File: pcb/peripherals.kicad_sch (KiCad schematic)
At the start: 12 parts, among them J10 SPI, J14 SERIAL, J3 INDICATOR, J8 QWIIC1, J9 QWIIC2, Q1 MMBT2222A

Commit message: Cleaned up fab layer. Minor tweaks. Updated renders.
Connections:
- net GND: now also J14.3; no longer J14.1
- net RX: now also J14.2; no longer J14.3
- net TX: now also J14.1; no longer J14.2
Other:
- moved on the sheet: J9
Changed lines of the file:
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@@
-	(wire
-		(pts
-			(xy 116.84 30.48) (xy 125.73 30.48)
-		)
-		(stroke
-			(width 0)
-			(type default)
-		)
-	)
 	(wire
 		(pts
@@
 	(wire
 		(pts
-			(xy 116.84 27.94) (xy 125.73 27.94)
-		)
-		(stroke
-			(width 0)
-			(type default)
-		)
-	)
-	(wire
-		(pts
 			(xy 238.76 38.1) (xy 238.76 39.37)
 		)
@@
 	(wire
 		(pts
+			(xy 116.84 30.48) (xy 124.46 30.48)
+		)
+		(stroke
+			(width 0)
+			(type default)
+		)
+	)
+	(wire
+		(pts
 			(xy 110.49 96.52) (xy 120.65 96.52)
 		)
@@
 	(wire
 		(pts
+			(xy 116.84 27.94) (xy 121.92 27.94)
+		)
+		(stroke
+			(width 0)
+			(type default)
+		)
+	)
+	(wire
+		(pts
 			(xy 207.01 60.96) (xy 207.01 67.31)
 		)
@@
 	(wire
 		(pts
-			(xy 54.61 54.61) (xy 68.58 54.61)
+			(xy 49.53 54.61) (xy 68.58 54.61)
 		)
 		(stroke
@@
 	(wire
 		(pts
-			(xy 54.61 52.07) (xy 68.58 52.07)
+			(xy 49.53 52.07) (xy 68.58 52.07)
+		)
+		(stroke
+			(width 0)
+			(type default)
+		)
+	)
+	(wire
+		(pts
+			(xy 116.84 25.4) (xy 121.92 25.4)
 		)
 		(stroke
@@
 	(global_label "RX"
 		(shape output)
-		(at 125.73 30.48 0)
+		(at 121.92 27.94 0)
 		(fields_autoplaced yes)
 		(effects
@@
 		)
 		(property "Intersheetrefs" "${INTERSHEET_REFS}"
-			(at 131.1947 30.48 0)
+			(at 127.3847 27.94 0)
 			(effects
 				(font
@@
 	(global_label "TX"
 		(shape input)
-		(at 125.73 27.94 0)
-		(fields_autoplaced yes)
+		(at 121.92 25.4 0)
 		(effects
 			(font
@@
 		)
 		(property "Intersheetrefs" "${INTERSHEET_REFS}"
-			(at 130.8923 27.94 0)
+			(at 126.492 25.4 0)
 			(effects
 				(font
@@
 	(symbol
 		(lib_id "power:GND")
-		(at 116.84 25.4 90)
+		(at 124.46 30.48 90)
 		(unit 1)
 		(exclude_from_sim no)
@@
 		(on_board yes)
 		(dnp no)
-		(fields_autoplaced yes)
 		(property "Reference" "#PWR028"
-			(at 123.19 25.4 0)
+			(at 130.81 30.48 0)
 			(effects
 				(font
@@
 		)
 		(property "Value" "GND"
-			(at 120.65 25.3999 90)
+			(at 127.762 30.48 90)
 			(effects
 				(font
@@
 		)
 		(property "Footprint" ""
-			(at 116.84 25.4 0)
+			(at 124.46 30.48 0)
 			(effects
 				(font
@@
 		)
 		(property "Datasheet" ""
-			(at 116.84 25.4 0)
+			(at 124.46 30.48 0)
 			(effects
 				(font
@@
 		)
 		(property "Description" "Power symbol creates a global label with name \"GND\" , ground"
-			(at 116.84 25.4 0)
+			(at 124.46 30.48 0)
 			(effects
 				(font
@@
 	(symbol
 		(lib_id "power:+3.3V")
-		(at 54.61 57.15 270)
+		(at 49.53 57.15 270)
 		(unit 1)
 		(exclude_from_sim no)
@@
 		(fields_autoplaced yes)
 		(property "Reference" "#PWR077"
-			(at 50.8 57.15 0)
+			(at 45.72 57.15 0)
 			(effects
 				(font
@@
 		)
 		(property "Value" "+3.3V"
-			(at 58.42 57.1499 90)
+			(at 53.34 57.1499 90)
 			(effects
 				(font
@@
 		)
 		(property "Footprint" ""
-			(at 54.61 57.15 0)
+			(at 49.53 57.15 0)
 			(effects
 				(font
@@
 		)
 		(property "Datasheet" ""
-			(at 54.61 57.15 0)
+			(at 49.53 57.15 0)
 			(effects
 				(font
@@
 		)
 		(property "Description" "Power symbol creates a global label with name \"+3.3V\""
-			(at 54.61 57.15 0)
+			(at 49.53 57.15 0)
 			(effects
 				(font
@@
 	(symbol
 		(lib_id "CRGM Connector:QWIIC")
-		(at 41.91 49.53 0)
+		(at 36.83 49.53 0)
 		(unit 1)
 		(exclude_from_sim no)
@@
 		(dnp no)
 		(property "Reference" "J9"
-			(at 46.482 45.72 0)
+			(at 41.402 45.72 0)
 			(effects
 				(font
@@
 		)
 		(property "Value" "QWIIC2"
-			(at 46.355 48.26 0)
+			(at 41.275 48.26 0)
 			(effects
 				(font
@@
 		)
 		(property "Footprint" "CRGM Connector:JST_SH_BM04B-SRSS-TB_1x04-1MP_P1.00mm_Vertical"
-			(at 41.91 49.53 0)
+			(at 36.83 49.53 0)
 			(effects
 				(font
@@
 		)
 		(property "Datasheet" "https://jlcpcb.com/partdetail/Hdgc-1_0K_BH4PB/C2919601"
-			(at 41.91 49.53 0)
+			(at 36.83 49.53 0)
 			(effects
 				(font
@@
 		)
 		(property "Description" "JST SH 1.0mm 4 Position Vertical"
-			(at 41.91 49.53 0)
+			(at 36.83 49.53 0)
 			(effects
 				(font
@@
 		)
 		(property "MPN" "BM04B-SRSS-TB"
-			(at 41.91 49.53 0)
+			(at 36.83 49.53 0)
 			(effects
 				(font
@@
 		)
 		(property "MN" "JST"
-			(at 41.91 49.53 0)
+			(at 36.83 49.53 0)
 			(effects
 				(font
@@
 		)
 		(property "LCSC" "C2919601"
-			(at 41.91 49.53 0)
+			(at 36.83 49.53 0)
 			(effects
 				(font
@@
 		)
 		(property "Mouser" "306-BM04BSRSSTBTLFSN"
-			(at 41.91 49.53 0)
+			(at 36.83 49.53 0)
 			(effects
 				(font
@@
 		)
 		(property "Digikey" "455-BM04B-SRSS-TBTR-ND"
-			(at 41.91 49.53 0)
+			(at 36.83 49.53 0)
 			(effects
 				(font
@@
 	(symbol
 		(lib_id "power:GND")
-		(at 54.61 59.69 90)
+		(at 49.53 59.69 90)
 		(unit 1)
 		(exclude_from_sim no)
@@
 		(fields_autoplaced yes)
 		(property "Reference" "#PWR078"
-			(at 60.96 59.69 0)
+			(at 55.88 59.69 0)
 			(effects
 				(font
@@
 		)
 		(property "Value" "GND"
-			(at 58.42 59.6899 90)
+			(at 53.34 59.6899 90)
 			(effects
 				(font
@@
 		)
 		(property "Footprint" ""
-			(at 54.61 59.69 0)
+			(at 49.53 59.69 0)
 			(effects
 				(font
@@
 		)
 		(property "Datasheet" ""
-			(at 54.61 59.69 0)
+			(at 49.53 59.69 0)
 			(effects
 				(font
@@
 		)
 		(property "Description" "Power symbol creates a global label with name \"GND\" , ground"
-			(at 54.61 59.69 0)
-			(effects
-				(font
+			(at 49.53 59.69 0)
+			(effects
+				(font

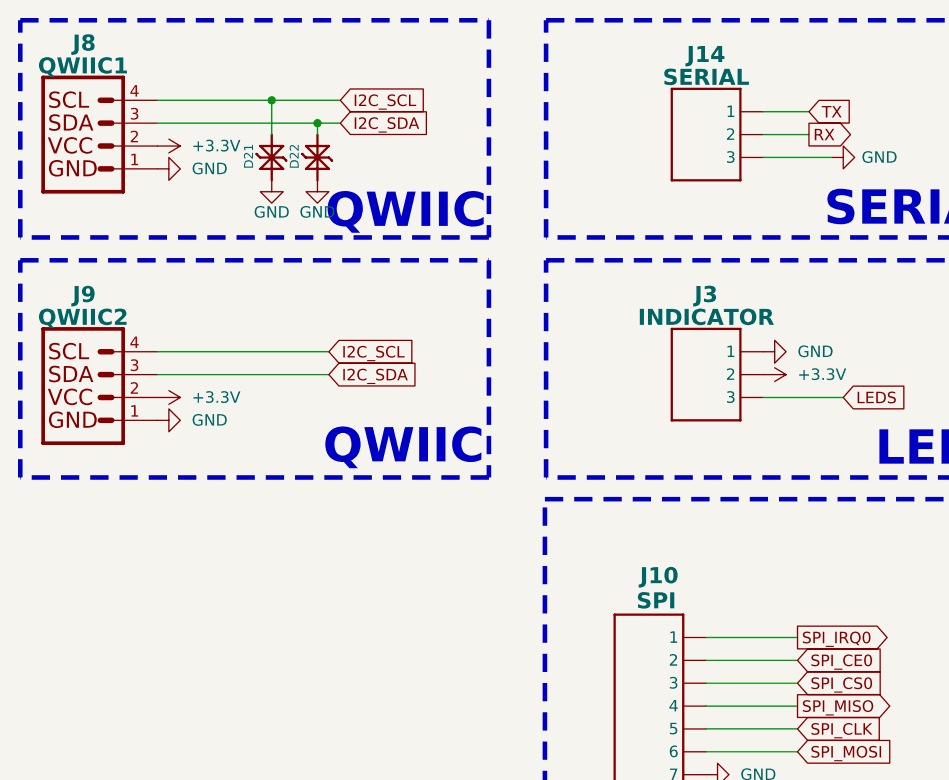
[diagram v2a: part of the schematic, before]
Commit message: closed #3 and #1
Fixed resistors and values
Widened panel
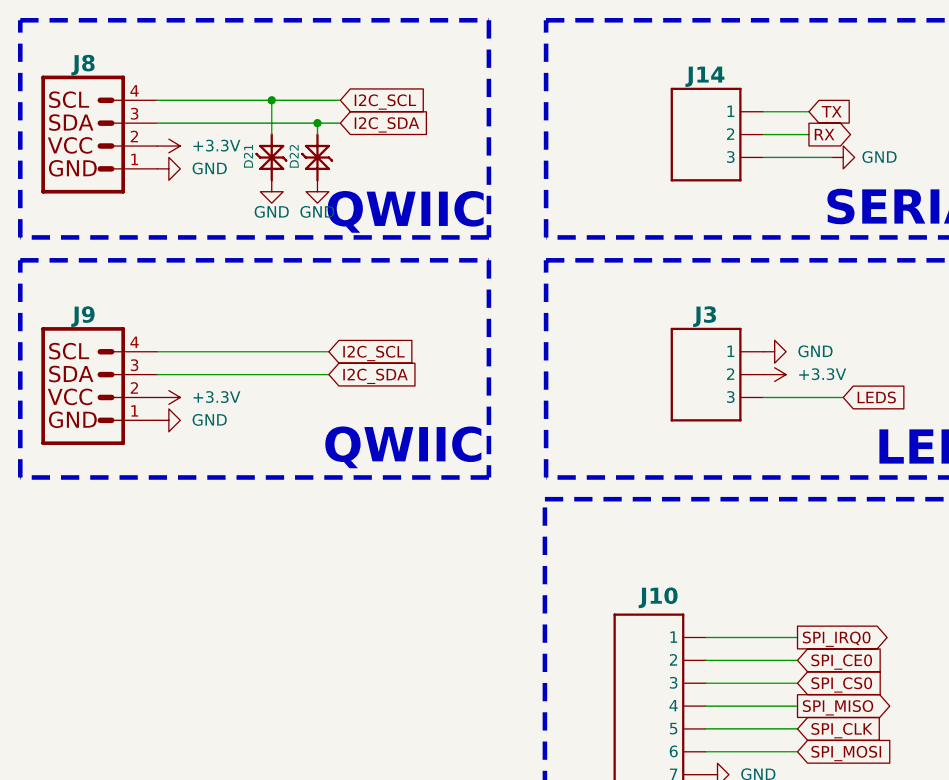
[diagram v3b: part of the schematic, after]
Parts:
- J10: value SPI -> BM08B-SRSS-TB
- J14: value SERIAL -> BM03B-SRSS-TB; footprint Connector_JST:JST_SH_BM03B-SRSS-TB_1x03-1MP_P1.00mm_Vertical -> CRGM Connector:JST_SH_BM03B-SRSS-TB_1x03-1MP_P1.00mm_Vertical
- J3: value INDICATOR -> BM03B-SRSS-TB
- J8: value QWIIC1 -> BM04B-SRSS-TB
- J9: value QWIIC2 -> BM04B-SRSS-TB
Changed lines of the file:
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@@
 	(title_block
 		(title "Aquarius")
-		(date "2025-02-12")
-		(rev "1.5")
+		(date "2025-06-22")
+		(rev "2.0")
 		(company "CRG Makes")
 	)
@@
 		(dnp no)
 		(property "Reference" "J9"
-			(at 41.402 45.72 0)
+			(at 41.402 48.006 0)
 			(effects
 				(font
@@
 			)
 		)
-		(property "Value" "QWIIC2"
+		(property "Value" "BM04B-SRSS-TB"
 			(at 41.275 48.26 0)
 			(effects
@@
 					(bold yes)
 				)
+				(hide yes)
 			)
 		)
@@
 		(dnp no)
 		(property "Reference" "J14"
-			(at 110.49 19.05 0)
+			(at 110.49 21.336 0)
 			(effects
 				(font
@@
 			)
 		)
-		(property "Value" "SERIAL"
+		(property "Value" "BM03B-SRSS-TB"
 			(at 110.49 21.59 0)
 			(effects
@@
 					(bold yes)
 				)
-			)
-		)
-		(property "Footprint" "Connector_JST:JST_SH_BM03B-SRSS-TB_1x03-1MP_P1.00mm_Vertical"
+				(hide yes)
+			)
+		)
+		(property "Footprint" "CRGM Connector:JST_SH_BM03B-SRSS-TB_1x03-1MP_P1.00mm_Vertical"
 			(at 113.03 16.51 0)
 			(effects
@@
 		(dnp no)
 		(property "Reference" "J10"
-			(at 107.442 76.962 0)
+			(at 107.442 79.248 0)
 			(effects
 				(font
@@
 			)
 		)
-		(property "Value" "SPI"
+		(property "Value" "BM08B-SRSS-TB"
 			(at 107.188 79.756 0)
 			(effects
@@
 				)
 				(justify left)
+				(hide yes)
 			)
 		)
@@
 		(dnp no)
 		(property "Reference" "J8"
-			(at 41.402 17.78 0)
+			(at 41.402 20.066 0)
 			(effects
 				(font
@@
 			)
 		)
-		(property "Value" "QWIIC1"
+		(property "Value" "BM04B-SRSS-TB"
 			(at 41.275 20.32 0)
 			(effects
@@
 					(bold yes)
 				)
+				(hide yes)
 			)
 		)
@@
 		(dnp no)
 		(property "Reference" "J3"
-			(at 110.49 45.72 0)
+			(at 110.49 48.006 0)
 			(effects
 				(font
@@
 			)
 		)
-		(property "Value" "INDICATOR"
+		(property "Value" "BM03B-SRSS-TB"
 			(at 110.49 48.26 0)
 			(effects
@@
 					(bold yes)
 				)
-			)
-		)
+				(hide yes)
+			)
+		)
